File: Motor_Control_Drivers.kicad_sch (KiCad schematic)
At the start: 4 parts, among them J901 SEI-125-02-GF-S-M-AT, J902 SEI-115-02-GF-S-M-AT

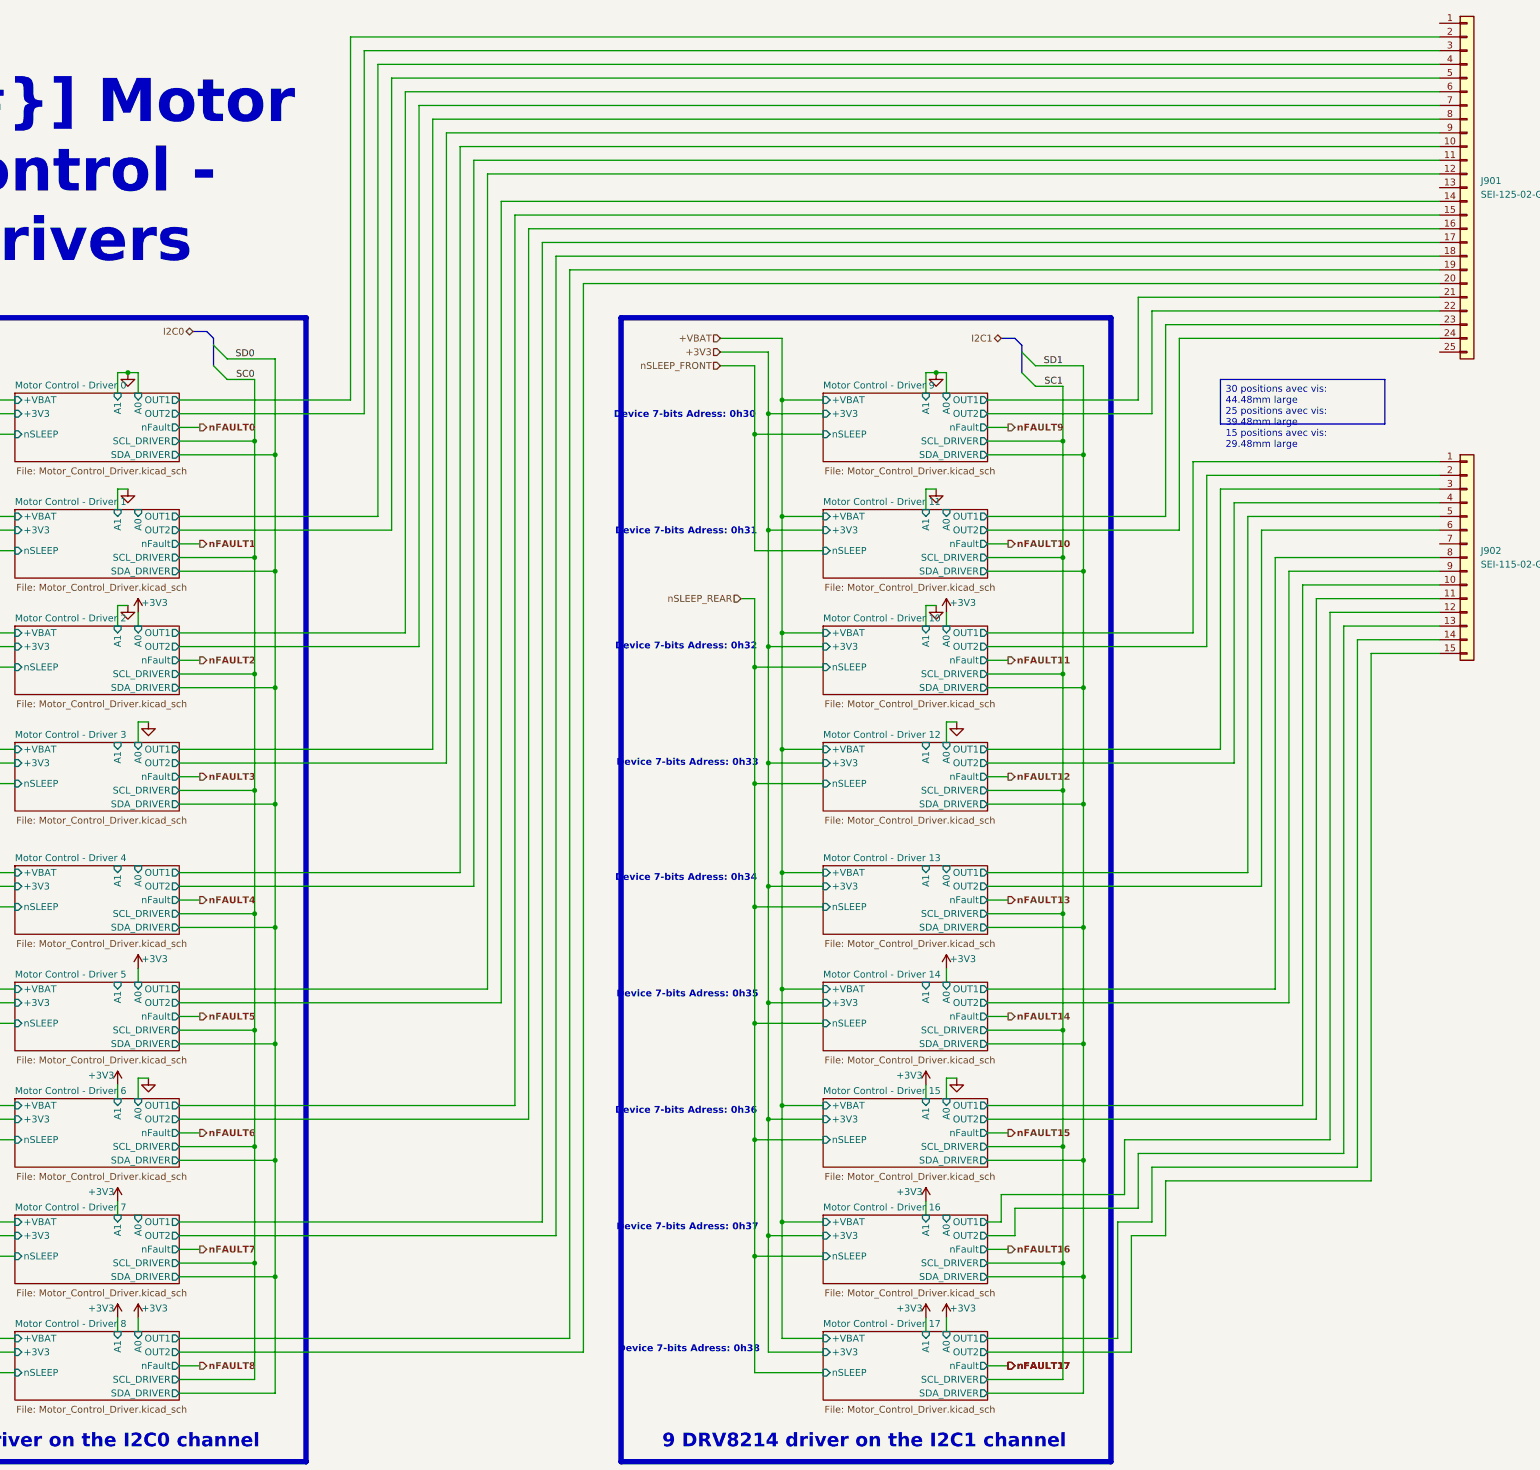
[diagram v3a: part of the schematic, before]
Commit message: Reviewed shematic, cleaned all DRC errors, chosed stackup, started layout
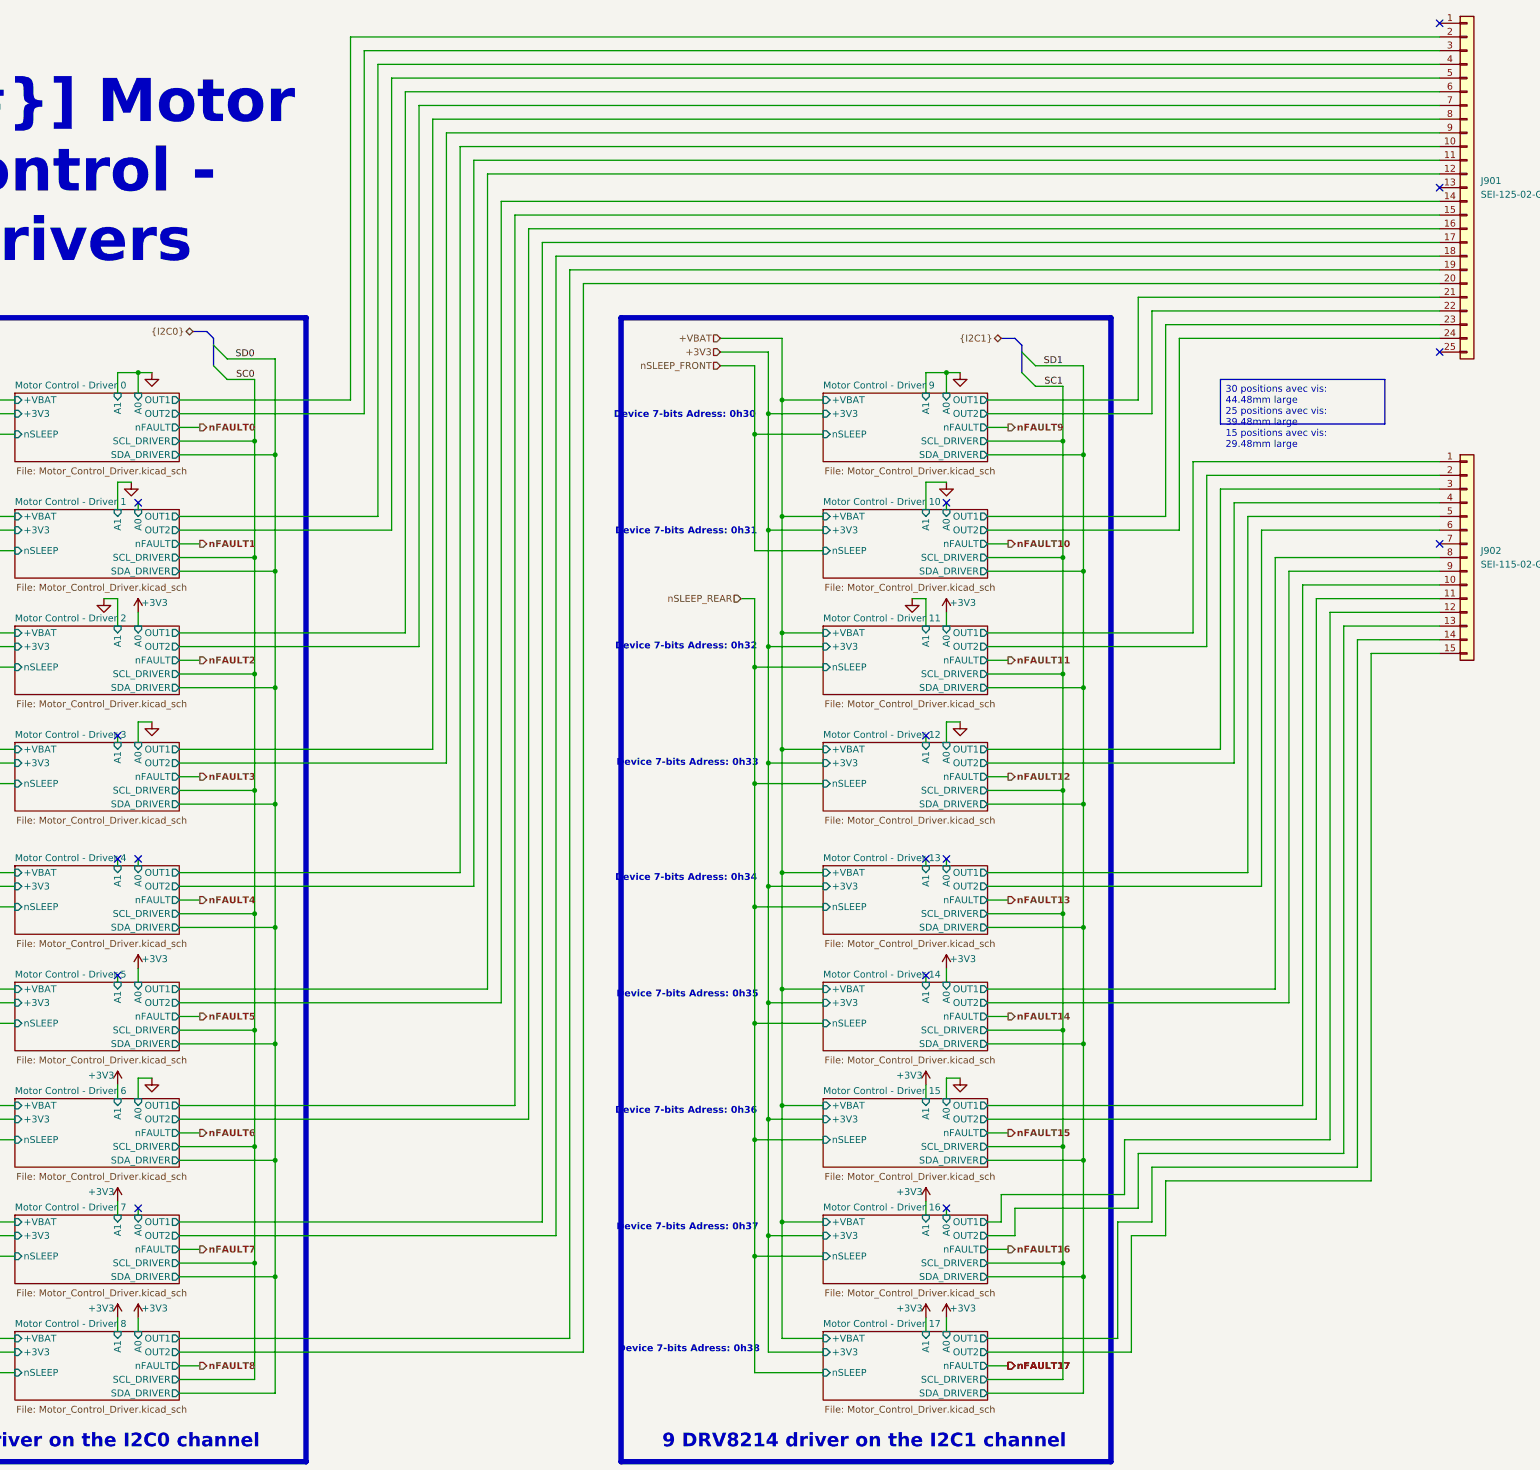
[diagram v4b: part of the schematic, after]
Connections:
- net Motor Control - Driver 10/OUT1: now also J901.23 (Pin_23); no longer J902.1 (Pin_1)
- net Motor Control - Driver 10/OUT2: now also J901.24 (Pin_24); no longer J902.2 (Pin_2)
- net Motor Control - Driver 11/OUT1: now also J902.1 (Pin_1); no longer J901.23 (Pin_23)
- net Motor Control - Driver 11/OUT2: now also J902.2 (Pin_2); no longer J901.24 (Pin_24)
- no-connect marks 0 -> 16
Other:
- sheet Motor Control - Driver 0 ports: added nFAULT; removed nFault
- sheet Motor Control - Driver 1 ports: added nFAULT; removed nFault
- sheet Motor Control - Driver 10 ports: added nFAULT; removed nFault
- sheet Motor Control - Driver 11 ports: added nFAULT; removed nFault
- sheet Motor Control - Driver 12 ports: added nFAULT; removed nFault
- sheet Motor Control - Driver 13 ports: added nFAULT; removed nFault
- sheet Motor Control - Driver 14 ports: added nFAULT; removed nFault
- sheet Motor Control - Driver 15 ports: added nFAULT; removed nFault
- sheet Motor Control - Driver 16 ports: added nFAULT; removed nFault
- sheet Motor Control - Driver 17 ports: added nFAULT; removed nFault
- sheet Motor Control - Driver 2 ports: added nFAULT; removed nFault
- sheet Motor Control - Driver 3 ports: added nFAULT; removed nFault
- sheet Motor Control - Driver 4 ports: added nFAULT; removed nFault
- sheet Motor Control - Driver 5 ports: added nFAULT; removed nFault
- sheet Motor Control - Driver 6 ports: added nFAULT; removed nFault
- sheet Motor Control - Driver 7 ports: added nFAULT; removed nFault
- sheet Motor Control - Driver 8 ports: added nFAULT; removed nFault
- sheet Motor Control - Driver 9 ports: added nFAULT; removed nFault

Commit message: Cleaned repo, cleaned and exported shematic, advanced rough layout
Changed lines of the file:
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@@
 	(title_block
 		(title "Motor Control - Drivers")
-		(date "2025-02-16")
+		(date "2025-04-05")
 		(rev "${REVISION}")
 		(company "${COMPANY}")
@@
 		)
 	)
+	(text_box "LAYOUT NOTE:\n\nUse the \"Replicate Layout\" KiCad Plugin to layout copy-paste the layout of each driver unit."
+		(exclude_from_sim no)
+		(at 354.33 150.495 0)
+		(size 48.895 23.495)
+		(margins 2.25 2.25 2.25 2.25)
+		(stroke
+			(width 1.016)
+			(type solid)
+			(color 0 0 255 1)
+		)
+		(fill
+			(type none)
+		)
+		(effects
+			(font
+				(face "Arial")
+				(size 2 2)
+				(thickness 0.4)
+				(bold yes)
+				(color 0 0 255 1)
+			)
+			(justify left top)
+		)
+	)
 	(text_box "[${#}] ${TITLE}"
 		(exclude_from_sim no)
@@
 			"AAAAAAAAAAAAAAAAAAAAAAAAAAAAAAAAAAAAAAAAAAAAAAAAAAAAAAAAAAAAAAAAAAAAAAAAAAAA"
 			"AAAAAAAAAAAAAAAAAAAAAAAAAAAAAAAAAAAAAAAAAAAAAAAAAAAAAAAAAAAAAAAAAAAAAAAAAAAA"
-			"AAAAAAAAAAAAAAAAAAAAAAAAAAAAAAAAAAAAAAAAAAAAAAAAAAAAAA=="
+			"AAAAAAAAAAAAAAAAAAAAAAAAAAAAAAAAAAAAAAAAAAAAAAAAAAAAAAAAAAAAAAAAAAAAAAAAAAAA"
+			"AAAAAAAAAAAAAAAAAAAAAAAAAAAAAAAAAAAAAAAAAAAAAAAAAAAAAAAAAAAAAAAAAAAAAAAAAAAA"
+			"AAAAAAAAAAAAAAAAAAAAAAAAAAAAAAAAAAAAAAAAAAAAAAAAAAAAAAAAAAAAAAAAAAAAAAAAAAAA"
+			"AAAAAAAAAAAAAAAAAAAAAAAAAAAAAAAAAAAAAAAAAAAAAAAAAAAAAAAAAAAAAAAAAAAAAAAAAAAA"
+			"AAAAAAAAAAAAAAAAAAAAAAAAAAAAAAAAAAAAAAAAAAAAAAAAAAAAAAAAAAAAAAAAAAAAAAAAAAAA"
+			"AAAAAAAAAAAAAAAAAAAAAAAAAAAAAAAAAAAAAAAAAAAAAAAAAAAAAAAAAAAAAAAAAAAAAAAAAAAA"
+			"AAAAAAAAAAAAAAAAAAAAAAAAAAAAAAAAAAAAAAAAAAAAAAAAAAAAAAAAAAAAAAAAAAAAAAAAAAAA"
+			"AAAAAAAAAAAAAAAAAAAAAAAAAAAAAAAAAAAAAAAAAAAAAAAAAAAAAAAAAAAAAAAAAAAAAAAAAAAA"
+			"AAAAAAAAAAAAAAAAAAAAAAAAAAAAAAAAAAAAAAAAAAAAAAAAAAAAAAAAAAAAAAAAAAAAAAAAAAAA"
+			"AAAAAAAAAAAAAAAAAAAAAAAAAAAAAAAAAAAAAAAAAAAAAAAAAAAAAAAAAAAAAAAAAAAAAAAAAAAA"
+			"AAAAAAAAAAAAAAAAAAAAAAAAAAAAAAAAAAAAAAAAAAAAAAAAAAAAAAAAAAAAAAAAAAAAAAAAAAAA"
+			"AAAAAAAAAAAAAAAAAAAAAAAAAAAAAAAAAAAAAAAAAAAAAAAAAAAAAAAAAAAAAAAAAAAAAAAAAAAA"
+			"AAAAAAAAAAAAAAAAAAAAAAAAAAAAAAAAAAAAAAAAAAAAAAAAAAAAAAAAAAAAAAAAAAAAAAAAAAAA"
+			"AAAAAAAAAAAAAAAAAAAAAAAAAAAAAAAAAAAAAAAAAAAAAAAAAAAAAAAAAAAAAAAAAAAAAAAAAAAA"
+			"AAAAAAAAAAAAAAAAAAAAAAAAAAAAAAAAAAAAAAAAAAAAAAAAAAAAAAAAAAAAAAAAAAAAAAAAAAAA"
+			"AAAAAAAAAAAAAAAAAAAAAAAAAAAAAAAAAAAAAAAAAAAAAAAAAAAAAAAAAAAAAAAAAAAAAAAAAAAA"
+			"AAAAAAAAAAAAAAAAAAAAAAAAAAAAAAAAAAAAAAAAAAAAAAAAAAAAAAAAAAAAAAAAAAAAAAAAAAAA"
+			"AAAAAAAAAAAAAAAAAAAAAAAAAAAAAAAAAAAAAAAAAAAAAAAAAAAAAAAAAAAAAAAAAAAAAAAAAAAA"
+			"AAAAAAAAAAAAAAAAAAAAAAAAAAAAAAAAAAAAAAAAAAAAAAAAAAAAAGlyeXdUcGx5ZWQvbVdWMFd4"
+			"emxiZml5eml6eGhlVlplOU1MZVB2V2VuM3pDSTcyMG5VVWNkRGNNN0orRGhRV1JhTm9jd3B2V3Q4"
+			"akJ0R0xtd0xQLzFwZUlkYktFczBOcHlFRFkrc1FqVW5qc3Y4VXUzZnRhNkVuaFJ5T1FFZVAwd2xQ"
+			"WFBveTIxVWFVSXJZWFhHNkgwSmF0ZmwrTDRnK2s3UWZMS1hiV2hzTm9MZEpYQ2JDZm03bkxkNUJx"
+			"NUFlamkxOVNsZGhPaGk1ak93eU1YTXZzdVBMLzQ1V1AvV3NpNmtHOXVJSE05UlJ0eThzZm5LbStm"
+			"a1A4WnZIN052UDFqV1B5TXVmd25aK2RubjNCeDlmUExzN05mbmorNCtzMkxGdzlmc3RuNmVoWTM1"
+			"UHB0K0ljdDhGc1hPUDd2Ly9PakI2OWVmZjZEbDFkWHY4KzA0dDlRSWY4YTUvc2h3OTJIWE5TYzMv"
+			"cFZrQ3hpK0lrMTcvQnpRZXBpQmhmdGVTUWxPeFc0SUdlWGdBTmZKdEkwSkY5RXBGL0VkZm14UWVZ"
+			"dnpzSzVzd1ZDbkVMSDZJbHVrc2xJTytUQ3BIQnpSdlBXc1lycmNIWG9PQzIwcFpmR0QweWNUL3JC"
+			"Yy9CYUE2UlFiYUVUQmNRK1BTdDVZb0R2MGM1MEJtc0hDa0VCTkpFVE9jS0pCUUV2MnZQeVZRY1Vr"
+			"SjFjS1ZjbXVTNWFzR1hwdk44OHhrNjVuUXF1NkZyTGN5WmlEa29zRnQya0kxQzMzb1czQVpXVENO"
+			"bzhGaU9KTFBBS0NlVlJGanFUZHFyaTJ5QXZxQTg3SG5lVzNQQ1lBOCtJWFhCY1BtSTNEZ01uaXh2"
+			"T0hWNi81b1ZxVE5pY1JMS3pDa3JJSHp6cFF4dWUwY2w4TzgwVngxQ3lUb2VLQkJyT1UyVkVwc0xa"
+			"b1FHa0hxdWVnZ2RjcEY2eWg0ejZSQ0VIZzNZc1VBTnkwc29LYmVDNmZSemhDYTJySkljb2RLQUlq"
+			"UzBPN1hoa1lRQ1B2MEEva3dEMVJENDFuL3p5bGIvU2xmY2l1MlFvclB6YitXb0tlUmFuY2hZbWFv"
+			"YVhkV1Flbkt4RHJjMGkyVDRKY0hHanE4TitKOXVWWWVXNHBxTjM2OXRiYno4NitSNlBwUHpnQno4"
+			"NCtiMS84VU4yYm53bmo2WTg0TnZhQnVXQS9EYmhIeG0wZzJYN0lLdU1lOGdrRjVqNm0zV25PWHEr"
+			"MGRDZTJDbTYxRnhJejkrcWY2bkYzaXNPUDRIQk93YnBhYk0zUXdhKzBLMk5XbDc3dVlDb3VTcVpj"
+			"WTlvc2YvRXRwV2hjc3FlcDdEcVJnZUdtNXptQWFSTTVtMjZraTZNcw=="
 		)
 	)

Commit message: Advanced rough layout
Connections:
- net Motor Control - Driver 0/OUT1 renamed OUT1_0
- net Motor Control - Driver 0/OUT2 renamed OUT2_0
- net Motor Control - Driver 1/OUT1 renamed OUT1_1
- net Motor Control - Driver 1/OUT2 renamed OUT2_1
- net Motor Control - Driver 10/OUT1 renamed OUT1_10
- net Motor Control - Driver 10/OUT2 renamed OUT2_10
- net Motor Control - Driver 11/OUT1 renamed OUT1_11
- net Motor Control - Driver 11/OUT2 renamed OUT2_11
- net Motor Control - Driver 12/OUT1 renamed OUT1_12
- net Motor Control - Driver 12/OUT2 renamed OUT2_12
- net Motor Control - Driver 13/OUT1 renamed OUT1_13
- net Motor Control - Driver 13/OUT2 renamed OUT2_13
- net Motor Control - Driver 14/OUT1 renamed OUT1_14
- net Motor Control - Driver 14/OUT2 renamed OUT2_14
- net Motor Control - Driver 15/OUT1 renamed OUT1_15
- net Motor Control - Driver 15/OUT2 renamed OUT2_15
- net Motor Control - Driver 16/OUT1 renamed OUT1_16
- net Motor Control - Driver 16/OUT2 renamed OUT2_16
- net Motor Control - Driver 17/OUT1 renamed OUT1_17
- net Motor Control - Driver 17/OUT2 renamed OUT2_17
- net Motor Control - Driver 2/OUT1 renamed OUT1_2
- net Motor Control - Driver 2/OUT2 renamed OUT2_2
- net Motor Control - Driver 3/OUT1 renamed OUT1_3
- net Motor Control - Driver 3/OUT2 renamed OUT2_3
- net Motor Control - Driver 4/OUT1 renamed OUT1_4
- net Motor Control - Driver 4/OUT2 renamed OUT2_4
- net Motor Control - Driver 5/OUT1 renamed OUT1_5
- net Motor Control - Driver 5/OUT2 renamed OUT2_5
- net Motor Control - Driver 6/OUT1 renamed OUT1_6
- net Motor Control - Driver 6/OUT2 renamed OUT2_6
- net Motor Control - Driver 7/OUT1 renamed OUT1_7
- net Motor Control - Driver 7/OUT2 renamed OUT2_7
- net Motor Control - Driver 8/OUT1 renamed OUT1_8
- net Motor Control - Driver 8/OUT2 renamed OUT2_8
- net Motor Control - Driver 9/OUT1 renamed OUT1_9
- net Motor Control - Driver 9/OUT2 renamed OUT2_9

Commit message: Finished layout, only cleaning left
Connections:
- net OUT1_14: now also J902.9 (Pin_9); no longer J902.8 (Pin_8)
- net OUT1_15: now also J902.11 (Pin_11); no longer J902.10 (Pin_10)
- net OUT2_14: now also J902.8 (Pin_8); no longer J902.9 (Pin_9)
- net OUT2_15: now also J902.10 (Pin_10); no longer J902.11 (Pin_11)

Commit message: Finished cleaning routing, removed errors, cleaned shematics, added pictures and other improvements
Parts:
- renumbered J901 to J1101, J902 to J1102, TP901 to TP1101, TP902 to TP1102
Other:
- note added: "x18"
